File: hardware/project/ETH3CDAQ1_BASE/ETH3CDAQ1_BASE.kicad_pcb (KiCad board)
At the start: 4 copper layers, 160 x 100 mm, 134 parts, among them J301 Conn_02x02_Odd_Even, J302 Conn_02x04_Odd_Even, J303 C64AC, J401 Conn_02x10_Odd_Even, J402 Conn_02x10_Odd_Even, J501 Conn_02x10_Odd_Even, J502 Conn_02x10_Odd_Even, J601 Conn_02x10_Odd_Even, J602 Conn_02x10_Odd_Even, Q201 IRFR5410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

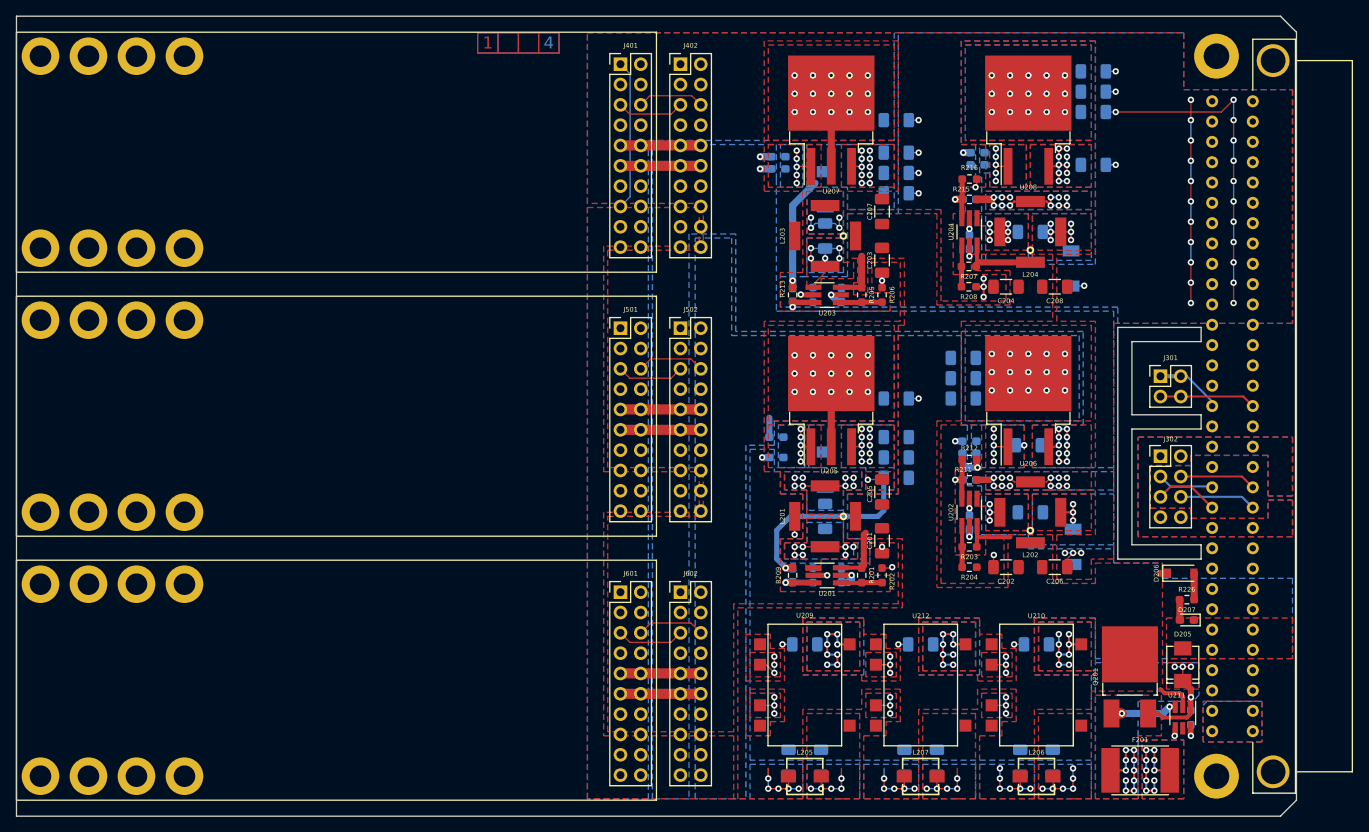
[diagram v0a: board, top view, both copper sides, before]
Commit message: Added selftest circuit in the base PCB.
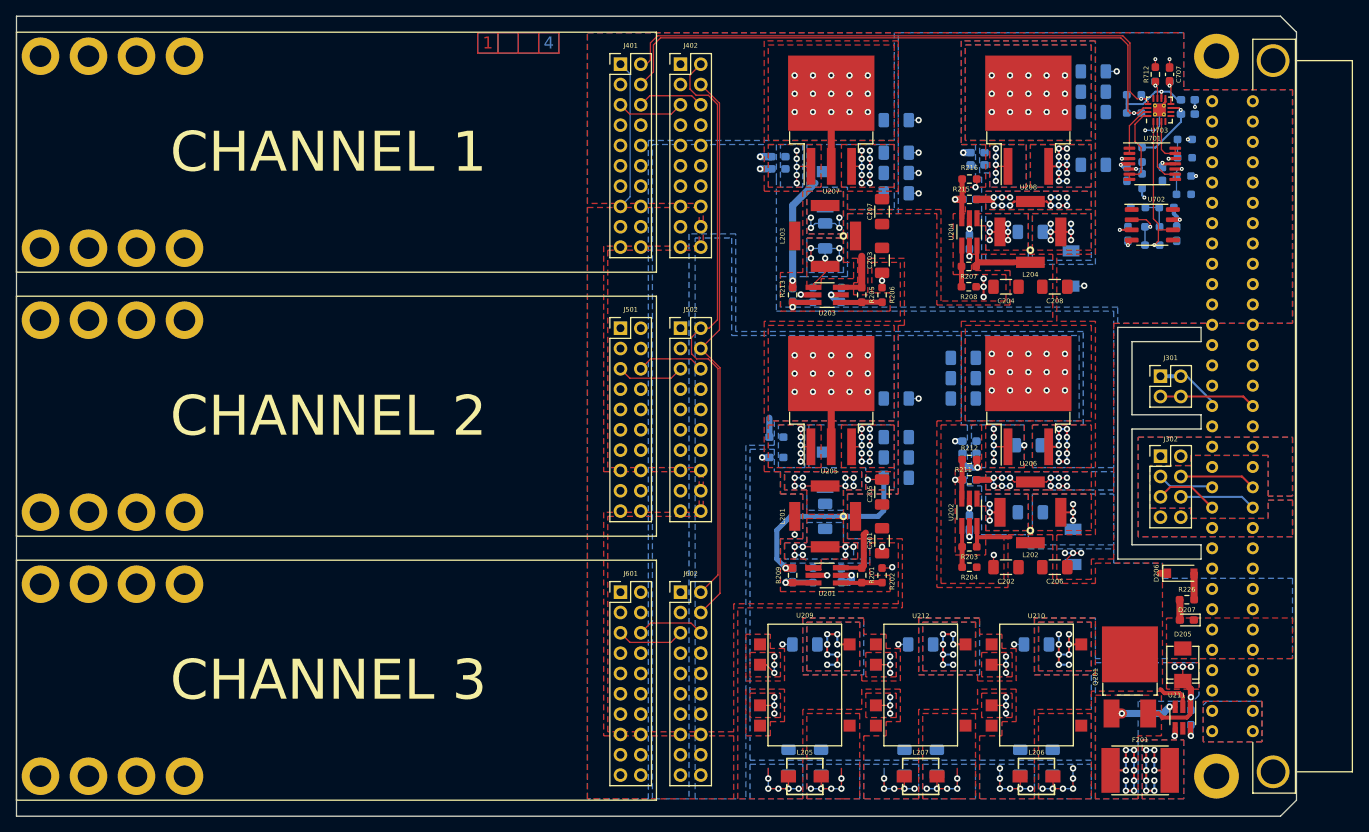
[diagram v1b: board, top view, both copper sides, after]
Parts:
- added C701: 100n, Capacitor_SMD:C_0603_1608Metric_Pad1.08x0.95mm_HandSolder, B.Cu at (201.8, 69.7)
- added C702: 100n, Capacitor_SMD:C_0603_1608Metric_Pad1.08x0.95mm_HandSolder, B.Cu at (201.9, 77.2)
- added C703: 100n, Capacitor_SMD:C_0603_1608Metric_Pad1.08x0.95mm_HandSolder, B.Cu at (208.0, 77.2)
- added C704: 100n, Capacitor_SMD:C_0603_1608Metric_Pad1.08x0.95mm_HandSolder, B.Cu at (206.2, 69.7)
- added C705: 100n, Capacitor_SMD:C_0603_1608Metric_Pad1.08x0.95mm_HandSolder, B.Cu at (209.4, 62.2)
- added C706: 100n, Capacitor_SMD:C_0603_1608Metric_Pad1.08x0.95mm_HandSolder, B.Cu at (209.4, 60.5)
- added C707: 1u, Capacitor_SMD:C_0603_1608Metric_Pad1.08x0.95mm_HandSolder, F.Cu at (207.1, 57.3)
- added R701: 200k, Resistor_SMD:R_0603_1608Metric_Pad0.98x0.95mm_HandSolder, B.Cu at (206.8, 73.9)
- added R702: 50k, Resistor_SMD:R_0603_1608Metric_Pad0.98x0.95mm_HandSolder, B.Cu at (203.2, 73.9)
- added R703: 200k, Resistor_SMD:R_0603_1608Metric_Pad0.98x0.95mm_HandSolder, B.Cu at (203.7, 67.3)
- added R704: 200k, Resistor_SMD:R_0603_1608Metric_Pad0.98x0.95mm_HandSolder, B.Cu at (208.9, 70.0)
- added R705: 200k, Resistor_SMD:R_0603_1608Metric_Pad0.98x0.95mm_HandSolder, B.Cu at (209.0, 65.4)
- added R706: 50k, Resistor_SMD:R_0603_1608Metric_Pad0.98x0.95mm_HandSolder, B.Cu at (203.7, 70.6)
- added R707: 50k, Resistor_SMD:R_0603_1608Metric_Pad0.98x0.95mm_HandSolder, B.Cu at (208.9, 72.3)
- added R708: 50k, Resistor_SMD:R_0603_1608Metric_Pad0.98x0.95mm_HandSolder, B.Cu at (209.0, 67.7)
- added R709: 1k, Resistor_SMD:R_0603_1608Metric_Pad0.98x0.95mm_HandSolder, B.Cu at (205.0, 76.3)
- added R710: 1k, Resistor_SMD:R_0603_1608Metric_Pad0.98x0.95mm_HandSolder, B.Cu at (205.0, 78.6)
- added R711: R, Resistor_SMD:R_0603_1608Metric_Pad0.98x0.95mm_HandSolder, B.Cu at (206.2, 58.2)
- added R712: R, Resistor_SMD:R_0603_1608Metric_Pad0.98x0.95mm_HandSolder, F.Cu at (205.4, 57.3)
- added R713: 4k7, Resistor_SMD:R_0603_1608Metric_Pad0.98x0.95mm_HandSolder, B.Cu at (202.7, 59.8)
- added R714: 4k7, Resistor_SMD:R_0603_1608Metric_Pad0.98x0.95mm_HandSolder, B.Cu at (202.7, 62.1)
- added U701: TL074, Package_SO:TSSOP-14_4.4x5mm_P0.65mm, F.Cu at (205.0, 68.5)
- added U702: TL071, Package_SO:SO-8_3.9x4.9mm_P1.27mm, F.Cu at (205.0, 76.1)
- added U703: TLA2528, Package_DFN_QFN:WQFN-16-1EP_3x3mm_P0.5mm_EP1.6x1.6mm_ThermalVias, F.Cu at (205.9, 61.7)
- renumbered H103 to H102, H104 to H103, H105 to H104, H102 to H105
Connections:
- J401 pad 2: /Channel 1/I2C_SCL -> /Channel 1/SCL
- J401 pad 4: /Channel 1/I2C_SDA -> /Channel 1/SDA
- J402 pad 2: /Channel 1/I2C_SCL -> /Channel 1/SCL
- J402 pad 4: /Channel 1/I2C_SDA -> /Channel 1/SDA
- J501 pad 2: /Channel 2/I2C_SCL -> /Channel 1/SCL
- J501 pad 4: /Channel 2/I2C_SDA -> /Channel 1/SDA
- J502 pad 2: /Channel 2/I2C_SCL -> /Channel 1/SCL
- J502 pad 4: /Channel 2/I2C_SDA -> /Channel 1/SDA
- J601 pad 2: /Channel 3/I2C_SCL -> /Channel 1/SCL
- J601 pad 4: /Channel 3/I2C_SDA -> /Channel 1/SDA
- J602 pad 2: /Channel 3/I2C_SCL -> /Channel 1/SCL
- J602 pad 4: /Channel 3/I2C_SDA -> /Channel 1/SDA
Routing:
- net /Channel 1/SCL: track 0.00 -> 173.3 mm, vias 0 -> 1
- net /Channel 1/SDA: track 0.00 -> 173.0 mm, vias 0 -> 1
- net +3V3: track 29.2 -> 130.1 mm, vias 8 -> 10
- net +18V: track 11.7 -> 88.8 mm, vias 15 -> 18
- net +9V: track 10.4 -> 87.1 mm, vias 8 -> 9
- net GND: track 148.0 -> 79.1 mm, vias 75 -> 56
- net -18V: track 26.9 -> 69.1 mm, vias 11 -> 13
- net +5V: track 10.4 -> 36.2 mm, vias 8 -> 9
- net /Selftest/AIN2: track 0.00 -> 18.4 mm, vias 0 -> 1
- net /Selftest/AIN1: track 0.00 -> 10.6 mm
- net /Selftest/AIN3: track 0.00 -> 8.93 mm
- net /Channel 3/I2C_SCL: track 8.47 -> 0.00 mm
- net /Channel 2/I2C_SCL: track 8.47 -> 0.00 mm
- net /Channel 1/I2C_SDA: track 8.47 -> 0.00 mm
- net /Channel 1/I2C_SCL: track 8.47 -> 0.00 mm
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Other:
- board text added: "CHANNEL 1"
- board text added: "CHANNEL 2"
- board text added: "CHANNEL 3"

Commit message: PCB design done
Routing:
- net Net-(C240-Pad1): vias 6 -> 5
- net +24VF: vias 16 -> 15

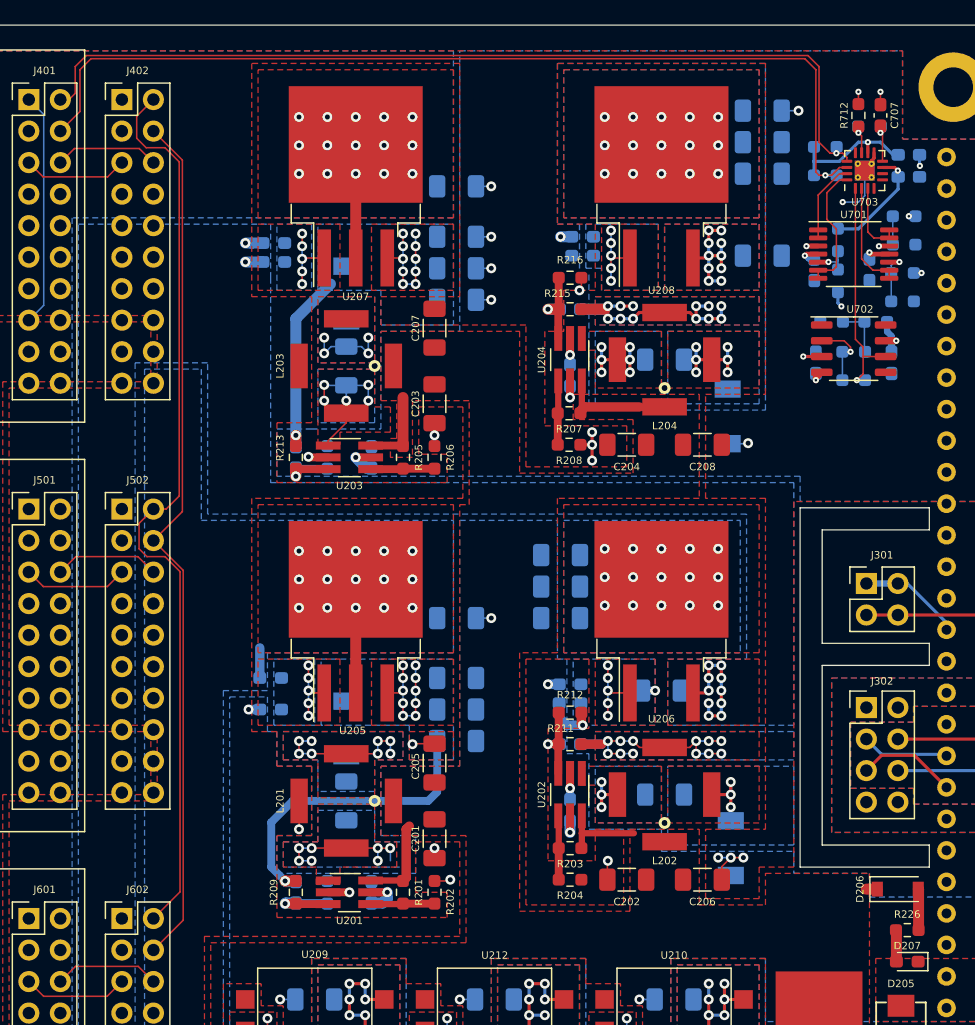
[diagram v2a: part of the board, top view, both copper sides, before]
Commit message: Modifications in PCB and schematic in the base module.
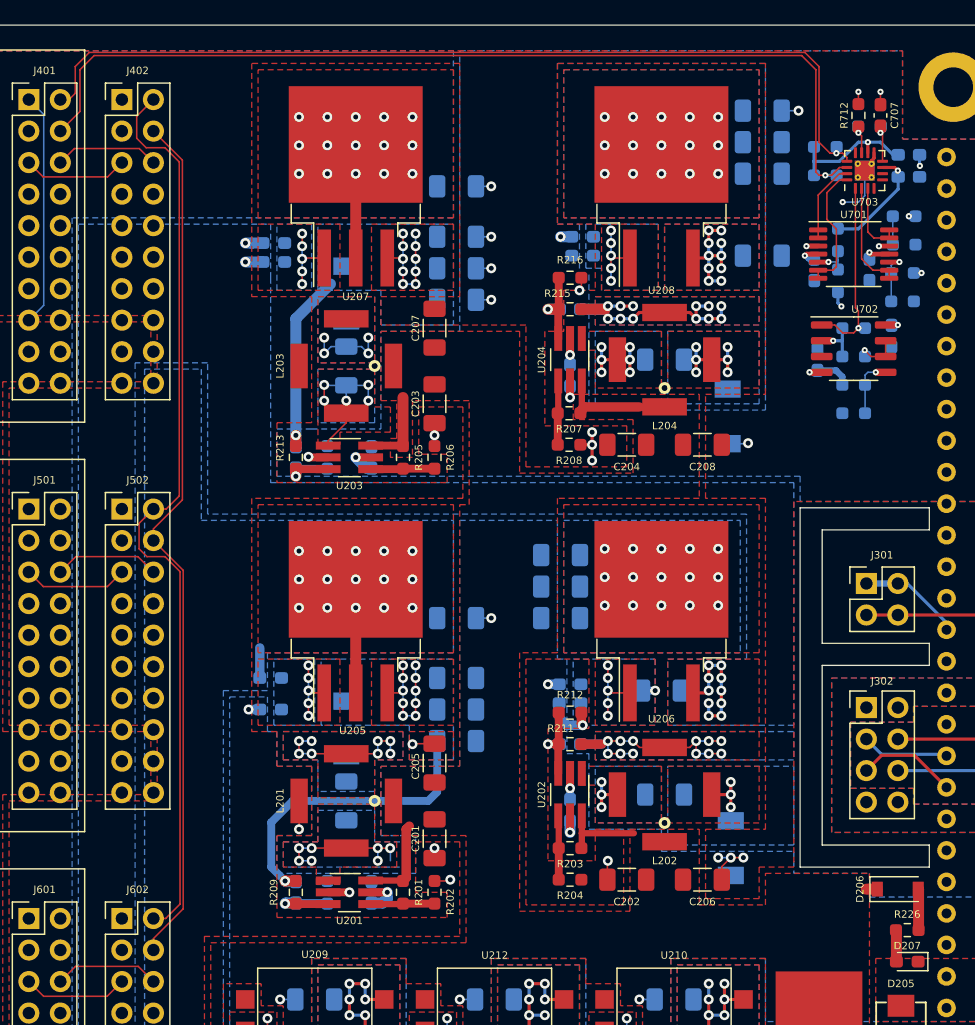
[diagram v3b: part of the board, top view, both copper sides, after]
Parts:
- R701, R705: value 200k -> 250k
- R703: value 200k -> 33k
- R704: value 200k -> 100k
- R711: value R -> 0
- R712: value R -> DNP
- U702: value TL071 -> TL072
- moved R702 7.58 mm to (205.0, 81.3)
- moved R701 5.38 mm to (205.0, 79.0), turned to 180 degrees
- moved R710 4.19 mm to (205.0, 74.4)
- moved C703 2.16 mm to (208.0, 75.1)
- moved R709 0.38 mm to (205.0, 76.7)
- moved C702 0.28 mm to (202.1, 77.0)
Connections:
- R701 pad 2: +18V -> -18V
- R709 pad 2: Net-(R701-Pad1) -> Net-(R709-Pad2)
- U702 pad 1: (no net) -> /Selftest/AIN2
- U702 pad 5: (no net) -> Net-(R701-Pad1)
- U702 pad 6: /Selftest/AIN2 -> Net-(R709-Pad2)
- U702 pad 7: +18V -> Net-(R709-Pad2)
- U702 pad 8: (no net) -> +18V
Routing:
- net +18V: track 88.8 -> 81.3 mm
- net -18V: track 69.1 -> 73.0 mm
- net Net-(R709-Pad2): track 0.00 -> 3.90 mm, vias 0 -> 1
- net /Selftest/AIN2: track 18.4 -> 15.3 mm
- net Net-(R709-Pad1): track 5.86 -> 3.99 mm
- net GND: track 79.1 -> 77.6 mm, vias 56 -> 55
- net /Channel 1/SCL: track 173.3 -> 174.0 mm
- net Net-(R701-Pad1): track 4.16 -> 4.83 mm, vias 0 -> 1
- net +9V: track 87.1 -> 86.6 mm
- added copper zone on In1.Cu, net +18V
- added copper zone on In1.Cu, net +9V

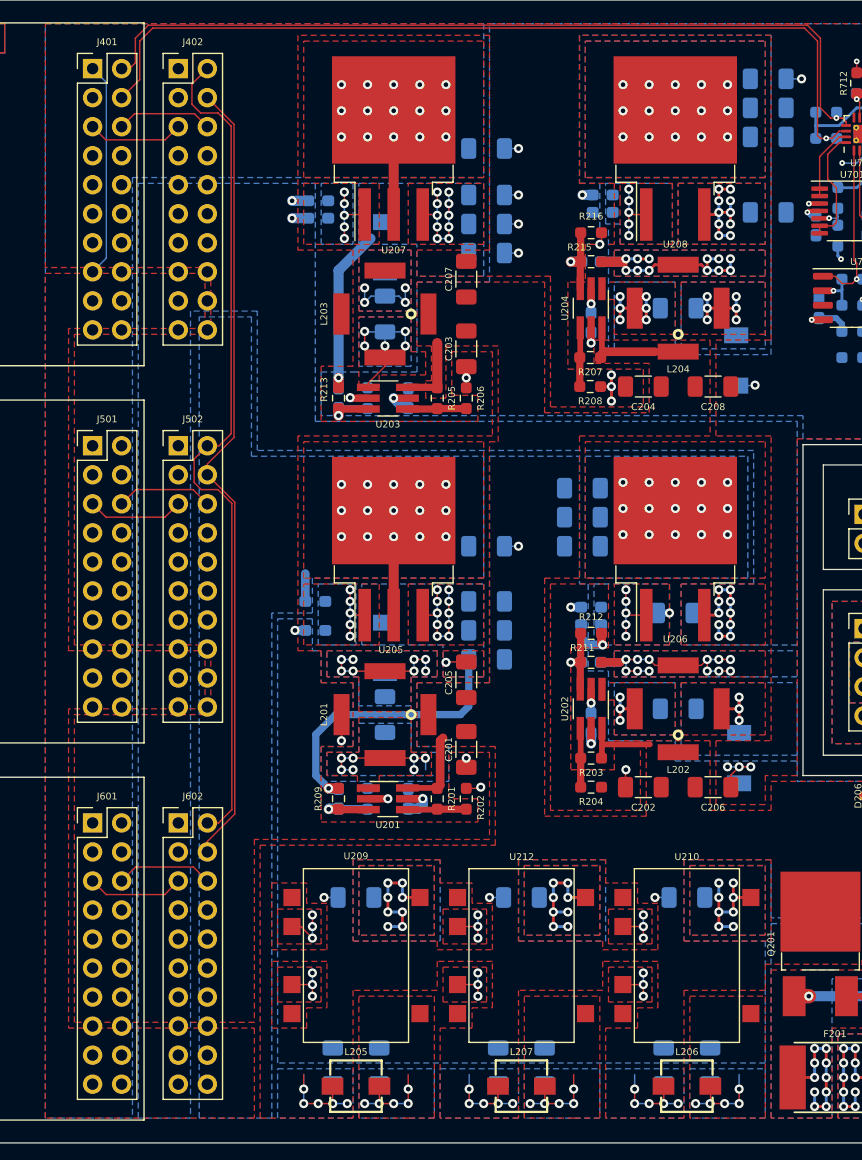
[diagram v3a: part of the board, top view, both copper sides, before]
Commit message: Base module PCB modifications.
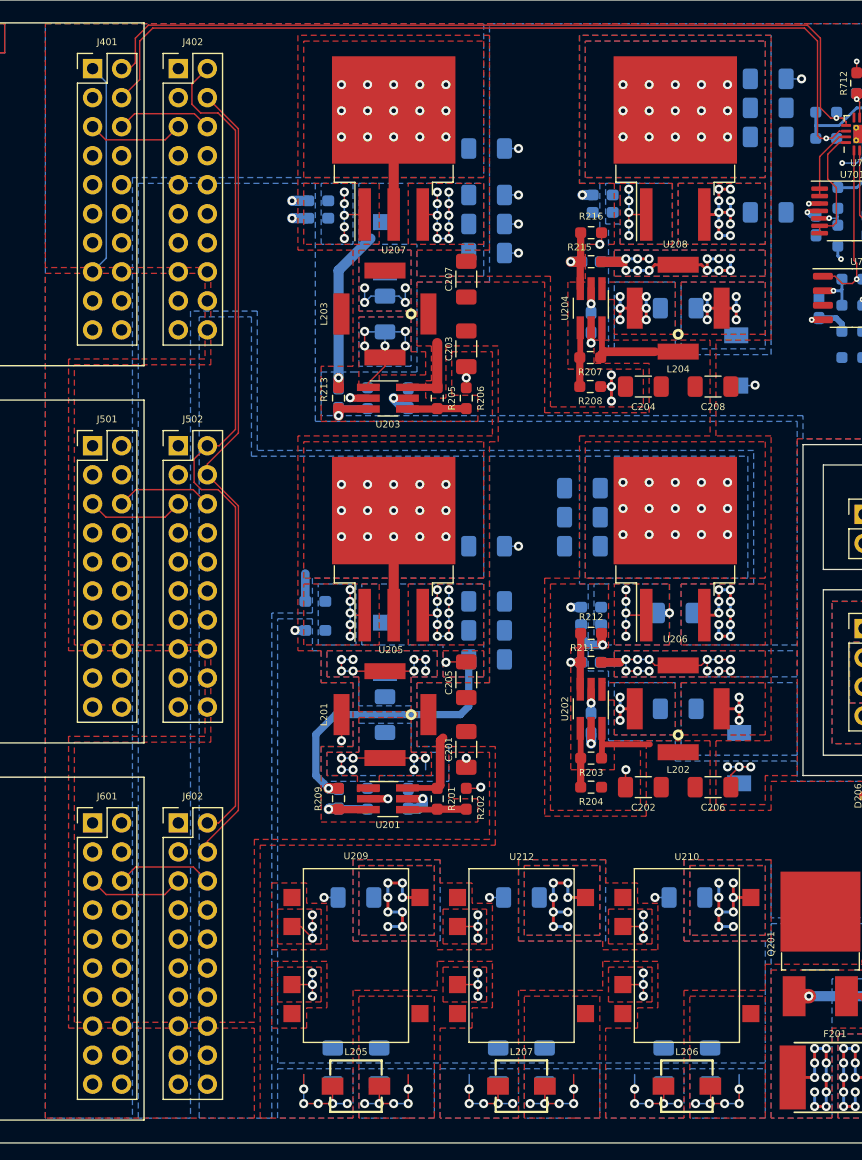
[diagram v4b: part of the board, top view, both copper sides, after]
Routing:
- net /Channel 1/SCL: track 174.0 -> 174.6 mm
- net /Channel 1/SDA: track 173.2 -> 173.8 mm

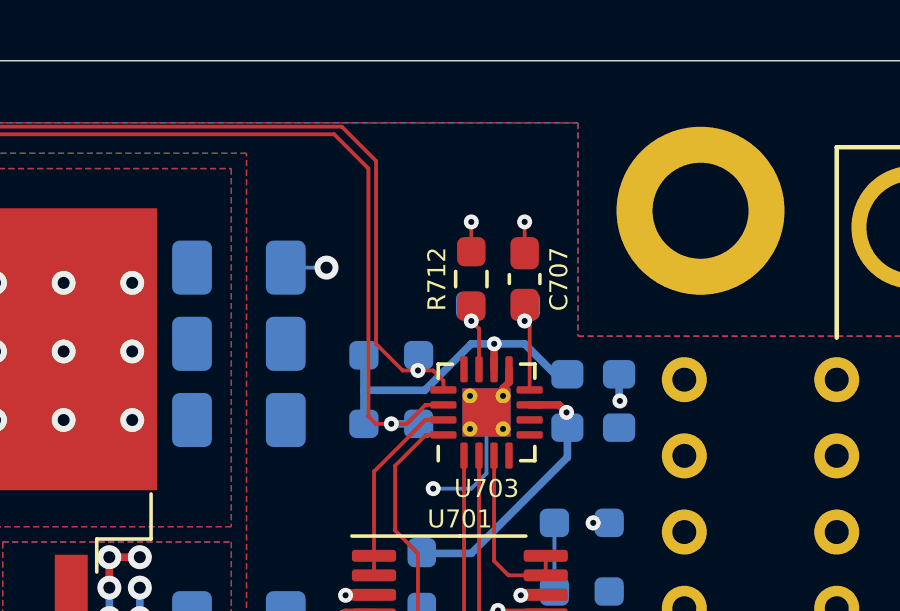
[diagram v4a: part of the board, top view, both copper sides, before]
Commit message: Modification in PCBs. Created BOM files.
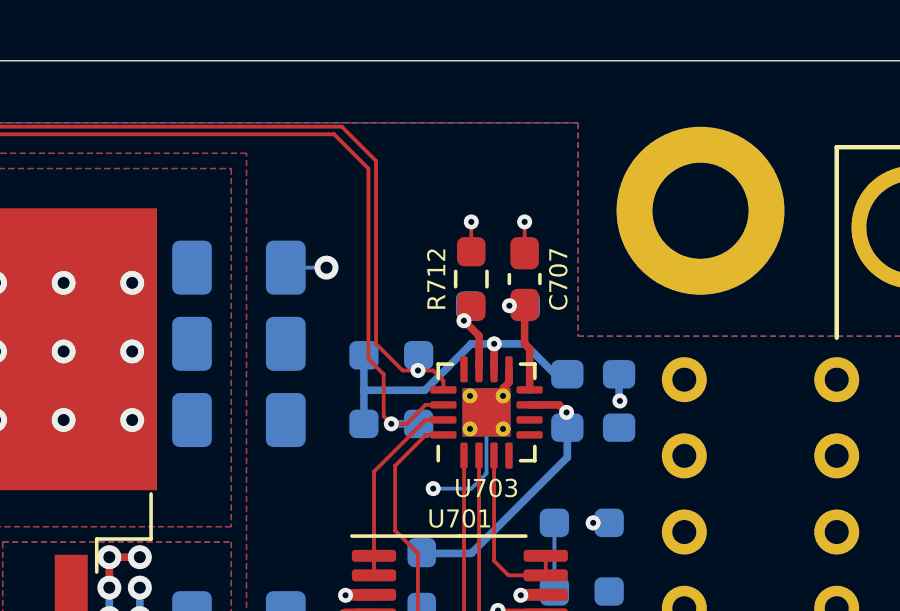
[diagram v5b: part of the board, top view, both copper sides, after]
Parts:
- C705: value 100n -> 1u
- R701, R705: value 250k -> 249k
- R702, R706, R707, R708: value 50k -> 49k9
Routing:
- net +3V3: track 130.1 -> 127.4 mm
- net Net-(C707-Pad2): track 2.89 -> 3.95 mm

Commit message: PCB modifications
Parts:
- moved R225 0.51 mm to (209.8, 137.2)
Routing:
- net GND: track 77.6 -> 88.0 mm
- net Net-(Q201-Pad1): track 8.30 -> 17.0 mm
- net Net-(R225-Pad2): track 2.34 -> 1.43 mm
- net Net-(D205-Pad1): track 28.5 -> 27.8 mm
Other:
- board text added: "ETH3CDAQ1_BASE V1.01"
